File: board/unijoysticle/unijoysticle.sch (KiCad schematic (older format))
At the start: 10 parts, among them J1 DB9_Female, J2 DB9_Female, J3 Barrel_Jack, SW1 SW_SPDT, U1 4066, U2 4066, U4 4066, U5 4066

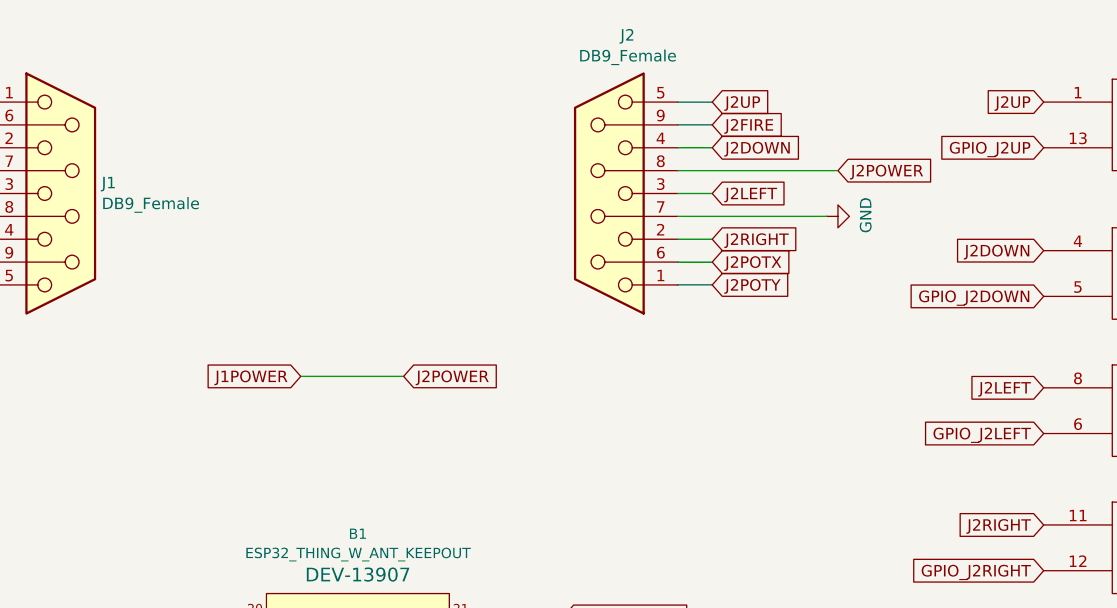
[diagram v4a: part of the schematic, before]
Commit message: board: autorouting ok. j1 & j2 connected correctly
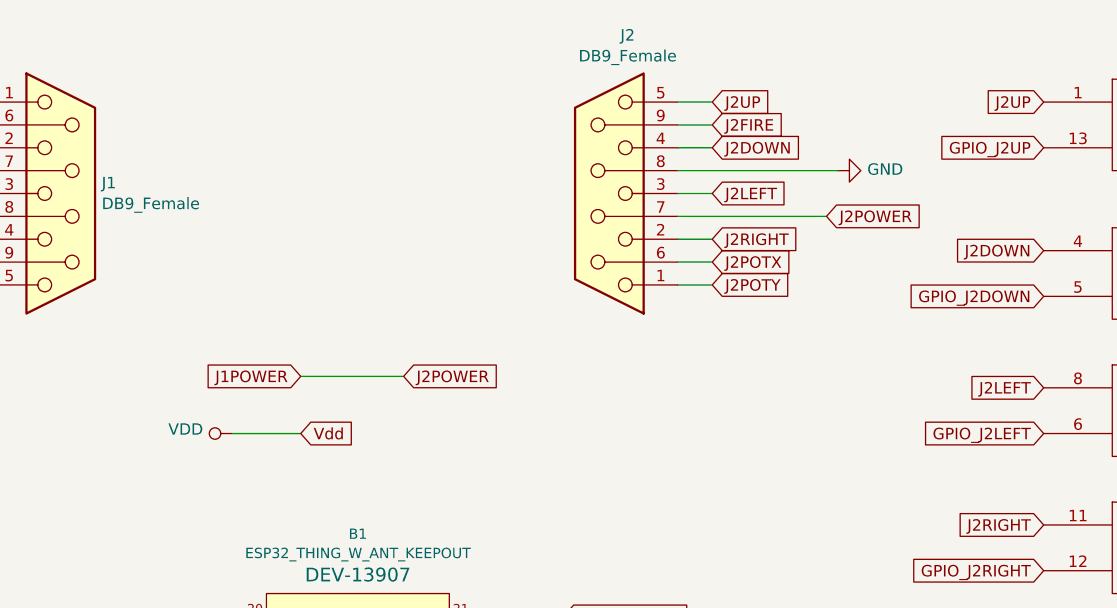
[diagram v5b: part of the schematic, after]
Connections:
- net Vdd is gone; now on net VDD: U1.14 (Vdd), U1.14 (Vdd), U1.14 (Vdd), U1.14 (Vdd), U2.14 (Vdd), U2.14 (Vdd), U2.14 (Vdd), U4.14 (Vdd), U4.14 (Vdd), U4.14 (Vdd), U4.14 (Vdd), U5.14 (Vdd), U5.14 (Vdd), U5.14 (Vdd)
- net GND: now also J2.8; no longer J2.7
- net J1POWER: now also J2.7; no longer J2.8
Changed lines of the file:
@@
 	9250 1050 9250 1700
-$Comp
-L power:GND #PWR07
-U 1 1 5C68CCF3
-P 7300 1450
-F 0 "#PWR07" H 7300 1200 50  0001 C CNN
-F 1 "GND" H 7305 1277 50  0000 C CNN
-F 2 "" H 7300 1450 50  0001 C CNN
-F 3 "" H 7300 1450 50  0001 C CNN
-	1    7300 1450
-	0    -1   -1   0
-$EndComp
 $Comp
 L power:GND #PWR06
@@
 Text GLabel 9450 4250 2    50   Input ~ 0
 POWER_OR_GND
-Text GLabel 7350 1250 2    50   Input ~ 0
+Text GLabel 7300 1450 2    50   Input ~ 0
 J2POWER
 Text GLabel 5000 2150 0    50   Input ~ 0
@@
 Wire Wire Line
 	6800 1750 6650 1750
+$Comp
+L power:VDD #PWR0106
+U 1 1 5C70E1A1
+P 4700 2400
+F 0 "#PWR0106" H 4700 2250 50  0001 C CNN
+F 1 "VDD" V 4718 2527 50  0000 L CNN
+F 2 "" H 4700 2400 50  0001 C CNN
+F 3 "" H 4700 2400 50  0001 C CNN
+	1    4700 2400
+	0    -1   -1   0
+$EndComp
+Text GLabel 5000 2400 2    50   Input ~ 0
+Vdd
+Wire Wire Line
+	4700 2400 5000 2400
+$Comp
+L power:GND #PWR?
+U 1 1 5C70F861
+P 7350 1250
+F 0 "#PWR?" H 7350 1000 50  0001 C CNN
+F 1 "GND" V 7355 1122 50  0000 R CNN
+F 2 "" H 7350 1250 50  0001 C CNN
+F 3 "" H 7350 1250 50  0001 C CNN
+	1    7350 1250
+	0    -1   -1   0
+$EndComp
 $EndSCHEMATC

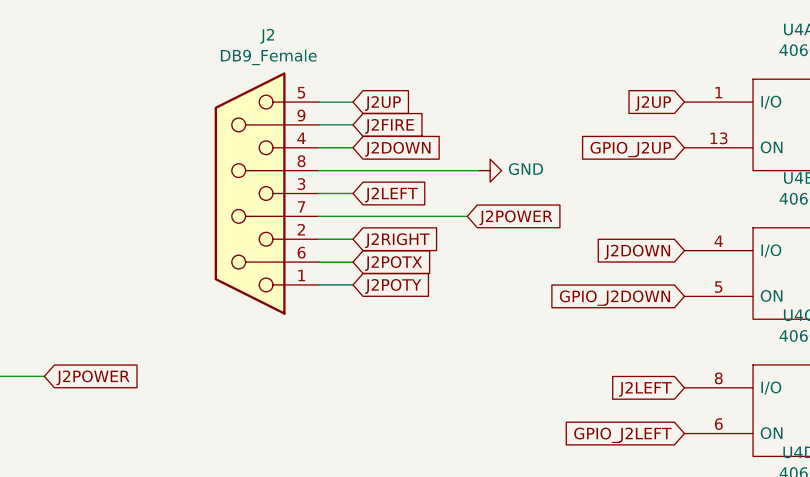
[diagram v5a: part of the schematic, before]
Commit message: board: logo re-added, c64/amiga legends and more
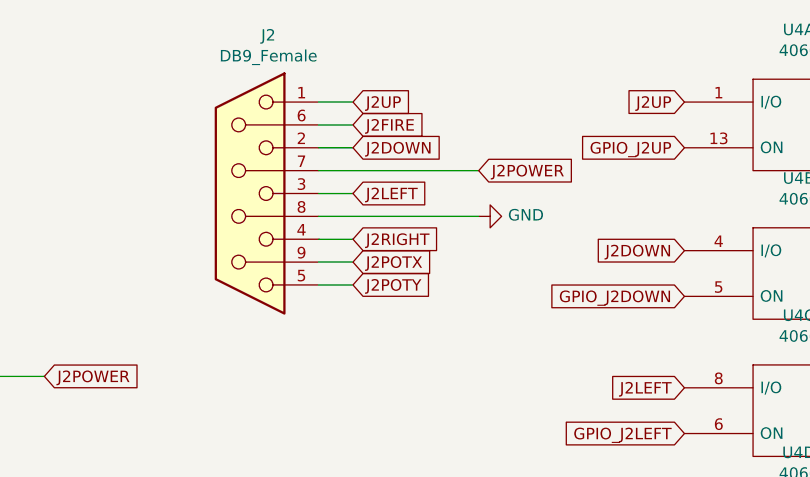
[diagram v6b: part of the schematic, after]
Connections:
- net J2DOWN: now also J2.2; no longer J2.4
- net J2FIRE: now also J2.6; no longer J2.9
- net J2POTX: now also J2.9; no longer J2.6
- net J2POTY: now also J2.5; no longer J2.1
- net J2RIGHT: now also J2.4; no longer J2.2
- net J2UP: now also J2.1; no longer J2.5
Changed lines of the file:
@@
 Text GLabel 9450 4250 2    50   Input ~ 0
 POWER_OR_GND
-Text GLabel 7300 1450 2    50   Input ~ 0
+Text GLabel 7350 1250 2    50   Input ~ 0
 J2POWER
 Text GLabel 5000 2150 0    50   Input ~ 0
@@
 U 1 1 5C705C0F
 P 6350 1350
-F 0 "J2" H 6270 658 50  0000 C CNN
-F 1 "DB9_Female" H 6270 749 50  0000 C CNN
+F 0 "J2" H 6270 2042 50  0000 C CNN
+F 1 "DB9_Female" H 6270 1951 50  0000 C CNN
 F 2 "Connector_Dsub:DSUB-9_Female_Horizontal_P2.77x2.84mm_EdgePinOffset9.40mm" H 6350 1350 50  0001 C CNN
 F 3 " ~" H 6350 1350 50  0001 C CNN
 	1    6350 1350
-	-1   0    0    1
+	-1   0    0    -1
 $EndComp
 Wire Wire Line
@@
 Wire Wire Line
 	6800 1350 6650 1350
-Wire Wire Line
-	6650 1450 7300 1450
 Wire Wire Line
 	6800 1550 6650 1550
@@
 Wire Wire Line
 	4700 2400 5000 2400
+Wire Wire Line
+	6650 1450 7350 1450
 $Comp
 L power:GND #PWR?
-U 1 1 5C70F861
-P 7350 1250
-F 0 "#PWR?" H 7350 1000 50  0001 C CNN
-F 1 "GND" V 7355 1122 50  0000 R CNN
-F 2 "" H 7350 1250 50  0001 C CNN
-F 3 "" H 7350 1250 50  0001 C CNN
-	1    7350 1250
+U 1 1 5C7111C5
+P 7350 1450
+F 0 "#PWR?" H 7350 1200 50  0001 C CNN
+F 1 "GND" V 7355 1322 50  0000 R CNN
+F 2 "" H 7350 1450 50  0001 C CNN
+F 3 "" H 7350 1450 50  0001 C CNN
+	1    7350 1450
 	0    -1   -1   0
 $EndComp

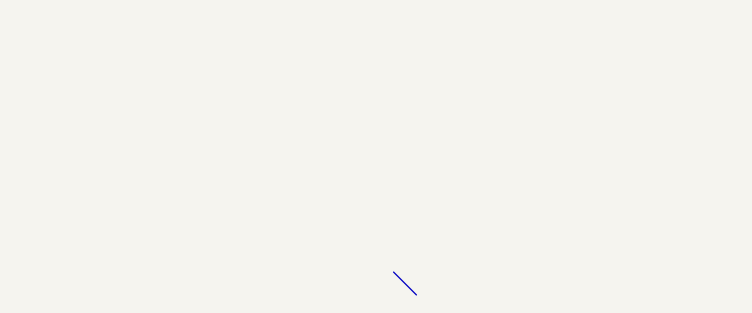
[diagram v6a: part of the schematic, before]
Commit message: firmware: WIP. add way to connect to undiscoverable devices
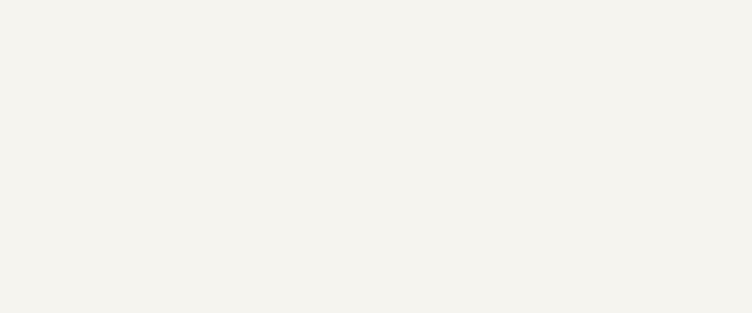
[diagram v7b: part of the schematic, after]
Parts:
- B1: footprint Parts:MH-ET_LIVE_MINIKIT_ESP32 -> ESP32_THING
- D1: footprint Diode_THT:D_DO-41_SOD81_P7.62mm_Horizontal -> Diode_THT:D_DO-41_SOD81_P10.16mm_Horizontal
- J1, J2: footprint Connector_Dsub:DSUB-9_Female_Horizontal_P2.77x2.84mm_EdgePinOffset9.40mm -> (none)
- J3: footprint Connector_BarrelJack:BarrelJack_Horizontal -> (none)
- SW1: footprint Button_Switch_THT:SW_CuK_OS102011MA1QN1_SPDT_Angled -> (none)
- U1, U2, U4, U5: footprint Package_DIP:DIP-14_W7.62mm_Socket_LongPads -> (none)
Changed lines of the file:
@@
 encoding utf-8
 Sheet 1 1
-Title ""
+Title "Unijoysticle 2"
 Date ""
-Rev ""
-Comp ""
+Rev "v0.0.1"
+Comp "Retro Moe"
 Comment1 ""
 Comment2 ""
@@
 F 0 "U1" H 1750 1466 50  0000 C CNN
 F 1 "4066" H 1750 1375 50  0000 C CNN
-F 2 "Package_DIP:DIP-14_W7.62mm_Socket_LongPads" H 1750 1050 50  0001 C CNN
+F 2 "" H 1750 1050 50  0001 C CNN
 F 3 "" H 1750 1050 50  0001 C CNN
 	1    1750 1050
@@
 F 0 "U1" H 1750 2116 50  0000 C CNN
 F 1 "4066" H 1750 2025 50  0000 C CNN
-F 2 "Package_DIP:DIP-14_W7.62mm_Socket_LongPads" H 1750 1700 50  0001 C CNN
+F 2 "" H 1750 1700 50  0001 C CNN
 F 3 "" H 1750 1700 50  0001 C CNN
 	2    1750 1700
@@
 F 0 "U1" H 1750 2666 50  0000 C CNN
 F 1 "4066" H 1750 2575 50  0000 C CNN
-F 2 "Package_DIP:DIP-14_W7.62mm_Socket_LongPads" H 1750 2250 50  0001 C CNN
+F 2 "" H 1750 2250 50  0001 C CNN
 F 3 "" H 1750 2250 50  0001 C CNN
 	3    1750 2250
@@
 F 0 "D1" H 2200 7116 50  0000 C CNN
 F 1 "1N4001" H 2200 7025 50  0000 C CNN
-F 2 "Diode_THT:D_DO-41_SOD81_P7.62mm_Horizontal" H 2200 6725 50  0001 C CNN
-F 3 "http://www.vishay.com/docs/88503/1n4001.pdf" H 2200 6900 50  0001 C CNN
+F 2 "Diode_THT:D_DO-41_SOD81_P10.16mm_Horizontal" H 2200 6725 50  0001 C CNN
+F 3 "" H 2200 6900 50  0001 C CNN
 	1    2200 6900
 	-1   0    0    -1
@@
 F 0 "U1" H 1750 3366 50  0000 C CNN
 F 1 "4066" H 1750 3275 50  0000 C CNN
-F 2 "Package_DIP:DIP-14_W7.62mm_Socket_LongPads" H 1750 2950 50  0001 C CNN
+F 2 "" H 1750 2950 50  0001 C CNN
 F 3 "" H 1750 2950 50  0001 C CNN
 	4    1750 2950
@@
 F 0 "U2" H 1750 4366 50  0000 C CNN
 F 1 "4066" H 1750 4275 50  0000 C CNN
-F 2 "Package_DIP:DIP-14_W7.62mm_Socket_LongPads" H 1750 3950 50  0001 C CNN
+F 2 "" H 1750 3950 50  0001 C CNN
 F 3 "" H 1750 3950 50  0001 C CNN
 	1    1750 3950
@@
 F 0 "U2" H 1750 4966 50  0000 C CNN
 F 1 "4066" H 1750 4875 50  0000 C CNN
-F 2 "Package_DIP:DIP-14_W7.62mm_Socket_LongPads" H 1750 4550 50  0001 C CNN
+F 2 "" H 1750 4550 50  0001 C CNN
 F 3 "" H 1750 4550 50  0001 C CNN
 	2    1750 4550
@@
 F 0 "U2" H 1750 5516 50  0000 C CNN
 F 1 "4066" H 1750 5425 50  0000 C CNN
-F 2 "Package_DIP:DIP-14_W7.62mm_Socket_LongPads" H 1750 5100 50  0001 C CNN
+F 2 "" H 1750 5100 50  0001 C CNN
 F 3 "" H 1750 5100 50  0001 C CNN
 	3    1750 5100
@@
 F 0 "U4" H 8750 1466 50  0000 C CNN
 F 1 "4066" H 8750 1375 50  0000 C CNN
-F 2 "Package_DIP:DIP-14_W7.62mm_Socket_LongPads" H 8750 1050 50  0001 C CNN
+F 2 "" H 8750 1050 50  0001 C CNN
 F 3 "" H 8750 1050 50  0001 C CNN
 	1    8750 1050
@@
 F 0 "U4" H 8750 2116 50  0000 C CNN
 F 1 "4066" H 8750 2025 50  0000 C CNN
-F 2 "Package_DIP:DIP-14_W7.62mm_Socket_LongPads" H 8750 1700 50  0001 C CNN
+F 2 "" H 8750 1700 50  0001 C CNN
 F 3 "" H 8750 1700 50  0001 C CNN
 	2    8750 1700
@@
 F 0 "U4" H 8750 2716 50  0000 C CNN
 F 1 "4066" H 8750 2625 50  0000 C CNN
-F 2 "Package_DIP:DIP-14_W7.62mm_Socket_LongPads" H 8750 2300 50  0001 C CNN
+F 2 "" H 8750 2300 50  0001 C CNN
 F 3 "" H 8750 2300 50  0001 C CNN
 	3    8750 2300
@@
 F 0 "U4" H 8750 3316 50  0000 C CNN
 F 1 "4066" H 8750 3225 50  0000 C CNN
-F 2 "Package_DIP:DIP-14_W7.62mm_Socket_LongPads" H 8750 2900 50  0001 C CNN
+F 2 "" H 8750 2900 50  0001 C CNN
 F 3 "" H 8750 2900 50  0001 C CNN
 	4    8750 2900
@@
 F 0 "U5" H 8750 4066 50  0000 C CNN
 F 1 "4066" H 8750 3975 50  0000 C CNN
-F 2 "Package_DIP:DIP-14_W7.62mm_Socket_LongPads" H 8750 3650 50  0001 C CNN
+F 2 "" H 8750 3650 50  0001 C CNN
 F 3 "" H 8750 3650 50  0001 C CNN
 	1    8750 3650
@@
 F 0 "U5" H 8750 4666 50  0000 C CNN
 F 1 "4066" H 8750 4575 50  0000 C CNN
-F 2 "Package_DIP:DIP-14_W7.62mm_Socket_LongPads" H 8750 4250 50  0001 C CNN
+F 2 "" H 8750 4250 50  0001 C CNN
 F 3 "" H 8750 4250 50  0001 C CNN
 	2    8750 4250
@@
 F 0 "U5" H 8750 5266 50  0000 C CNN
 F 1 "4066" H 8750 5175 50  0000 C CNN
-F 2 "Package_DIP:DIP-14_W7.62mm_Socket_LongPads" H 8750 4850 50  0001 C CNN
+F 2 "" H 8750 4850 50  0001 C CNN
 F 3 "" H 8750 4850 50  0001 C CNN
 	3    8750 4850
@@
 F 0 "B1" H 5250 5560 45  0000 C CNN
 F 1 "ESP32_THING_W_ANT_KEEPOUT" H 5250 5476 45  0000 C CNN
-F 2 "Parts:MH-ET_LIVE_MINIKIT_ESP32" H 5250 5400 20  0001 C CNN
+F 2 "ESP32_THING" H 5250 5400 20  0001 C CNN
 F 3 "" H 5250 4200 50  0001 C CNN
 F 4 "DEV-13907" H 5250 5381 60  0000 C CNN "Field4"
@@
 Wire Wire Line
 	4300 5000 4750 5000
-Entry Bus Bus
-	8750 7700 8850 7800
 $Comp
 L power:VDD #PWR0103
@@
 F 0 "SW1" H 1650 6085 50  0000 C CNN
 F 1 "SW_SPDT" H 1650 5994 50  0000 C CNN
-F 2 "Button_Switch_THT:SW_CuK_OS102011MA1QN1_SPDT_Angled" H 1650 5800 50  0001 C CNN
+F 2 "" H 1650 5800 50  0001 C CNN
 F 3 "" H 1650 5800 50  0001 C CNN
 	1    1650 5800
@@
 F 0 "J3" H 1555 7325 50  0000 C CNN
 F 1 "Barrel_Jack" H 1555 7234 50  0000 C CNN
-F 2 "Connector_BarrelJack:BarrelJack_Horizontal" H 1550 6960 50  0001 C CNN
-F 3 "~" H 1550 6960 50  0001 C CNN
+F 2 "" H 1550 6960 50  0001 C CNN
+F 3 "" H 1550 6960 50  0001 C CNN
 	1    1500 7000
 	1    0    0    -1
@@
 F 0 "J1" H 4129 1396 50  0000 L CNN
 F 1 "DB9_Female" H 4129 1305 50  0000 L CNN
-F 2 "Connector_Dsub:DSUB-9_Female_Horizontal_P2.77x2.84mm_EdgePinOffset9.40mm" H 3950 1350 50  0001 C CNN
-F 3 " ~" H 3950 1350 50  0001 C CNN
+F 2 "" H 3950 1350 50  0001 C CNN
+F 3 "" H 3950 1350 50  0001 C CNN
 	1    3950 1350
 	1    0    0    -1
@@
 F 0 "J2" H 6270 2042 50  0000 C CNN
 F 1 "DB9_Female" H 6270 1951 50  0000 C CNN
-F 2 "Connector_Dsub:DSUB-9_Female_Horizontal_P2.77x2.84mm_EdgePinOffset9.40mm" H 6350 1350 50  0001 C CNN
-F 3 " ~" H 6350 1350 50  0001 C CNN
+F 2 "" H 6350 1350 50  0001 C CNN
+F 3 "" H 6350 1350 50  0001 C CNN
 	1    6350 1350
 	-1   0    0    -1
@@
 	6650 1450 7350 1450
 $Comp
-L power:GND #PWR?
+L power:GND #PWR0108
 U 1 1 5C7111C5
 P 7350 1450
-F 0 "#PWR?" H 7350 1200 50  0001 C CNN
+F 0 "#PWR0108" H 7350 1200 50  0001 C CNN
 F 1 "GND" V 7355 1322 50  0000 R CNN
 F 2 "" H 7350 1450 50  0001 C CNN
